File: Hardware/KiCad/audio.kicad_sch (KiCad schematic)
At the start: 38 parts, among them IC1 LM4861M, J4 PJ-307C, J5 PJ-2282, SW1 PTT, U5 MAX9814

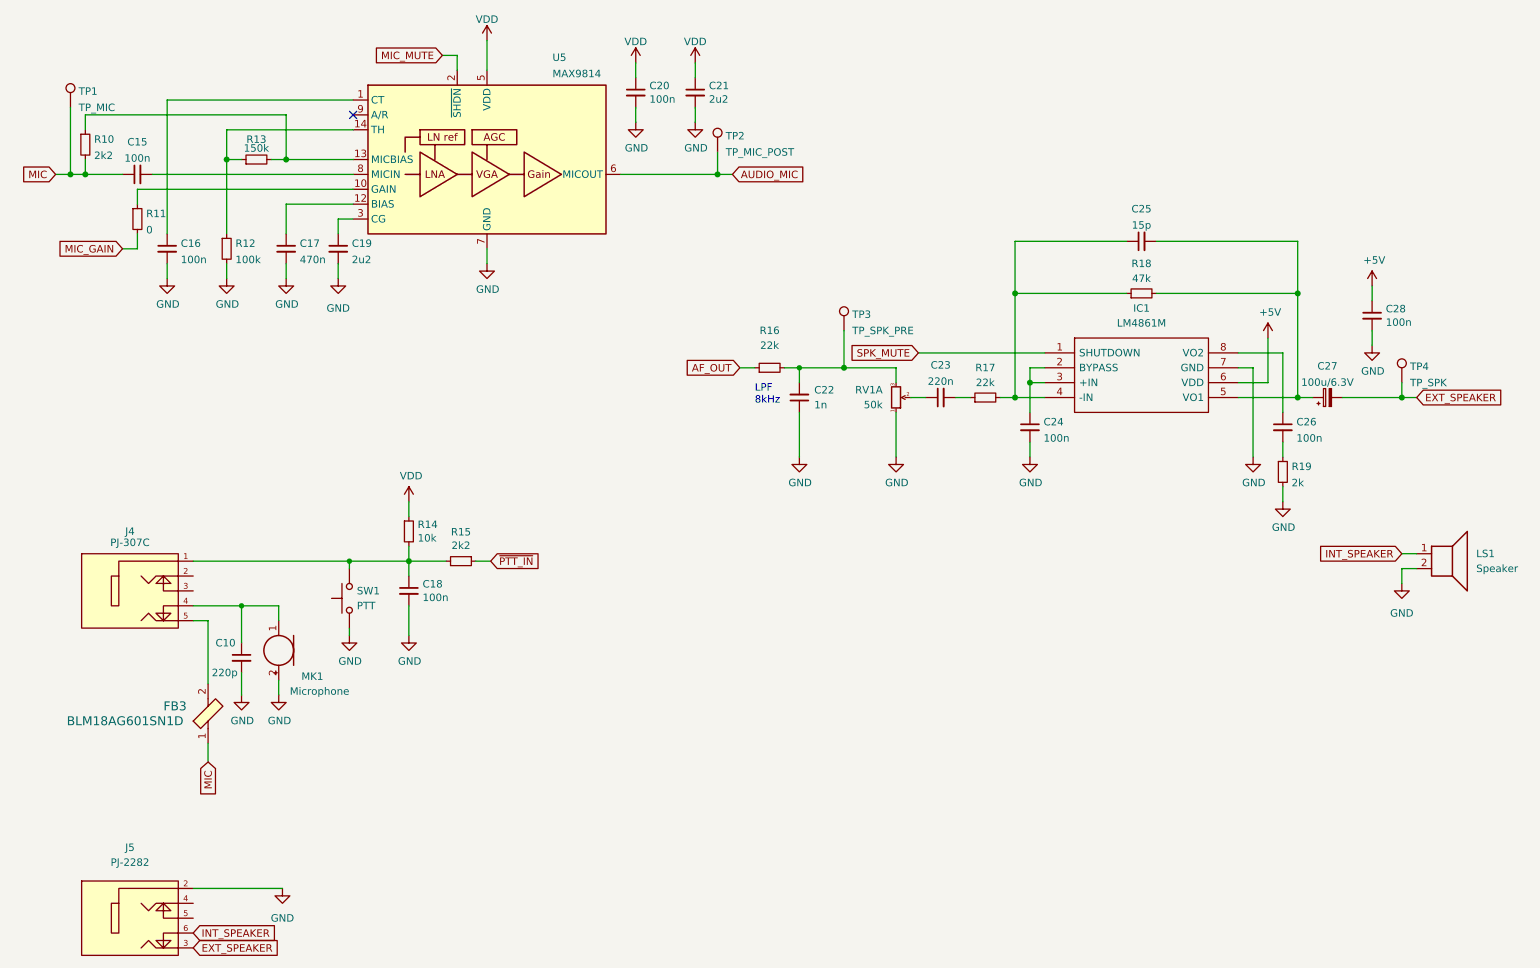
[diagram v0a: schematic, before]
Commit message: Schematic update
- nets for the internal speaker renamed
- encoder nets renamed, encoder circuit updated
- various other minor edits
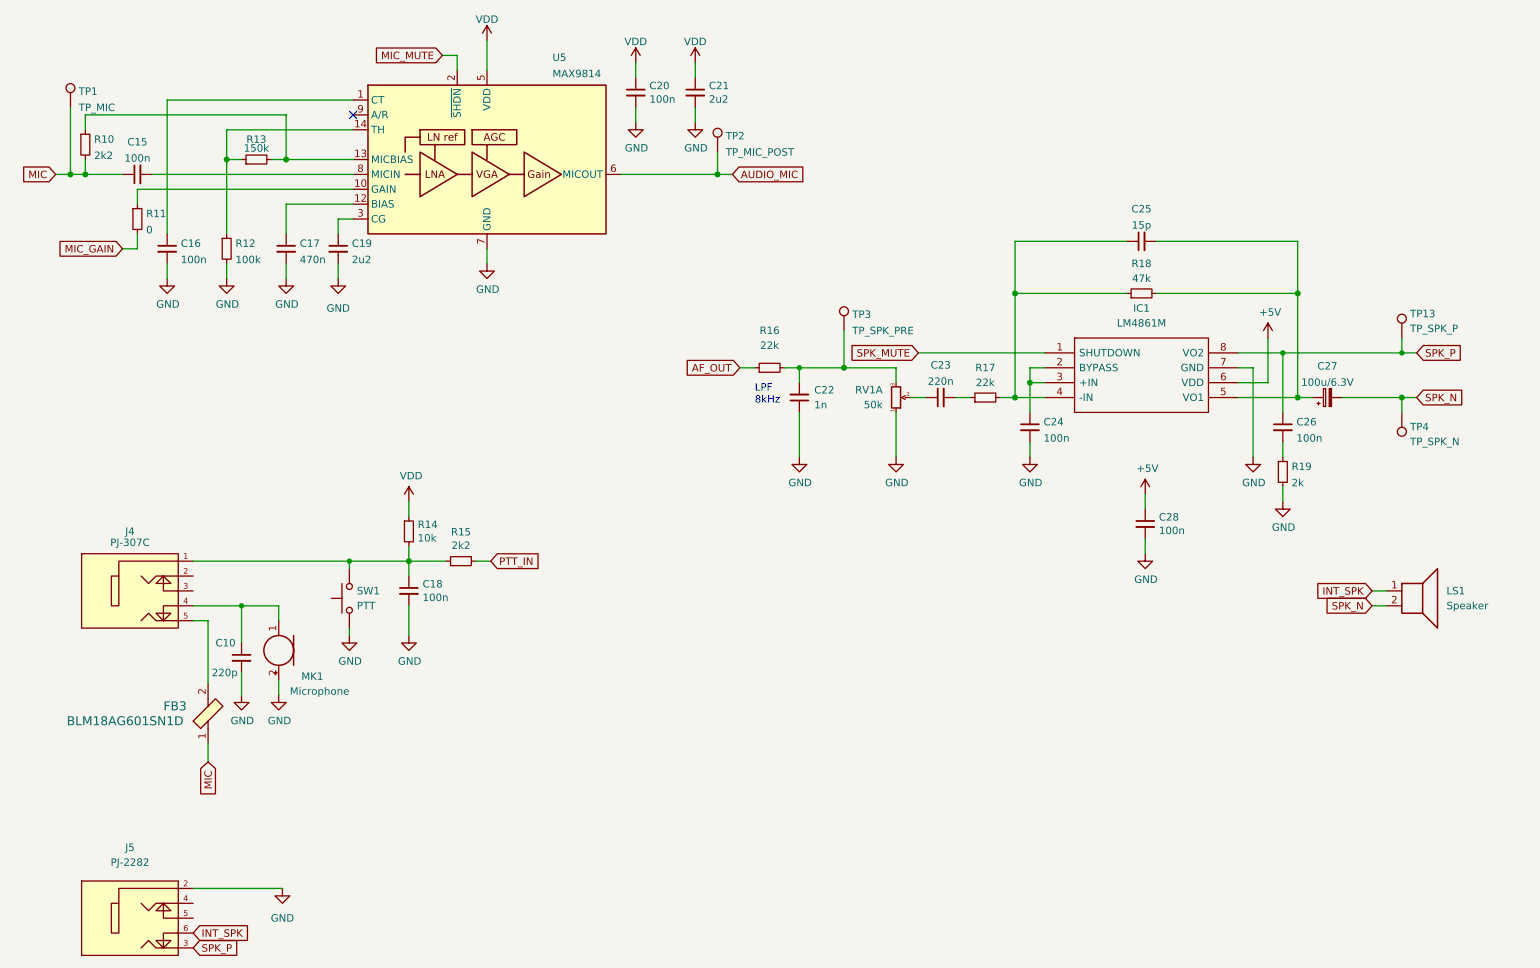
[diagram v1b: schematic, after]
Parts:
- added TP13: TP_SPK_P, TestPoint:TestPoint_Pad_D1.0mm, symbol Connector:TestPoint
- TP4: value TP_SPK -> TP_SPK_N
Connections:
- net GND: no longer LS1.2
- net SPK_P: now reaches C26.1, IC1.8 (VO2)
- net SPK_P: now also J5.3, TP13.1
- net EXT_SPEAKER renamed SPK_N
- net SPK_N: now also LS1.2; no longer J5.3
- net INT_SPEAKER renamed INT_SPK
- net ~{PTT_IN} renamed PTT_IN
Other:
- moved on the sheet: C28, LS1, TP4
